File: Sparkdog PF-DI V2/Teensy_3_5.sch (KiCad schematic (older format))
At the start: 4 parts, among them U300 Teensy_3_5

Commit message: Commit schematic changes, new parts library footprints and step files, PCB design file.
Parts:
- D300, D301: footprint (none) -> Samacsys:RESC2012X60N
- RN300: footprint (none) -> Samacsys:742C083103JP
- U300: footprint (none) -> Sparkdog PF-DI V2:TEENSY_3_5
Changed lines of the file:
@@
 F 0 "U300" H 5675 9115 50  0000 C CNN
 F 1 "Teensy_3_5" H 5675 9024 50  0000 C CNN
-F 2 "" H 5100 5350 50  0001 C CNN
+F 2 "Sparkdog PF-DI V2:TEENSY_3_5" H 5100 5350 50  0001 C CNN
 F 3 "" H 5100 5350 50  0001 C CNN
 	1    5100 5350
@@
 F 0 "RN300" H 3938 5996 50  0000 L CNN
 F 1 "1206 1k" H 3938 5905 50  0000 L CNN
-F 2 "" V 4025 5950 50  0001 C CNN
+F 2 "Samacsys:742C083103JP" V 4025 5950 50  0001 C CNN
 F 3 "~" H 3750 5950 50  0001 C CNN
 	1    3750 5950
@@
 F 0 "D300" H 4193 6295 50  0000 C CNN
 F 1 "0805 LED" H 4193 6386 50  0000 C CNN
-F 2 "" H 4200 6550 50  0001 C CNN
+F 2 "Samacsys:RESC2012X60N" H 4200 6550 50  0001 C CNN
 F 3 "~" H 4200 6550 50  0001 C CNN
 	1    4200 6550
@@
 F 0 "D301" H 4193 6745 50  0000 C CNN
 F 1 "0805 LED" H 4193 6836 50  0000 C CNN
-F 2 "" H 4200 7000 50  0001 C CNN
+F 2 "Samacsys:RESC2012X60N" H 4200 7000 50  0001 C CNN
 F 3 "~" H 4200 7000 50  0001 C CNN
 	1    4200 7000

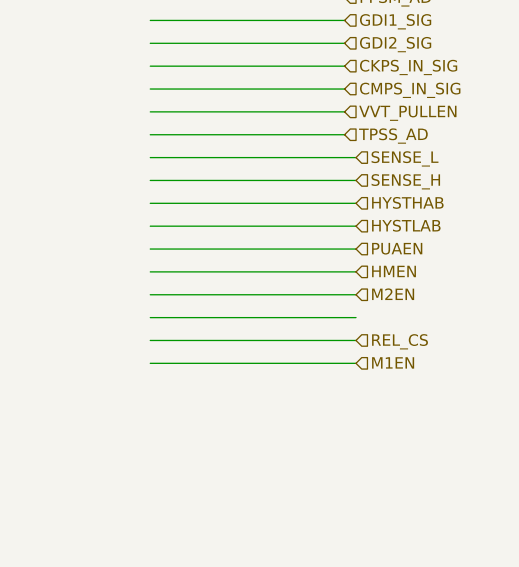
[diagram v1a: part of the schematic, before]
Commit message: Commit updates and Teensy schematic footprint correction.
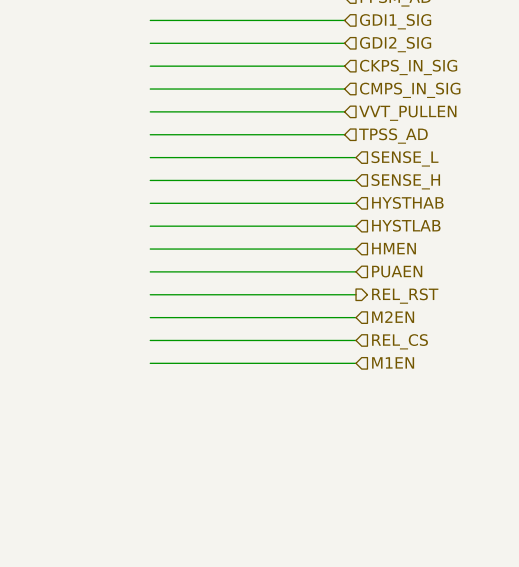
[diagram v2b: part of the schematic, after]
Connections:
- net labels added: REL_RST
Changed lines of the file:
@@
 Text HLabel 7350 4550 2    50   Input ~ 0
 HYSTLAB
+Text HLabel 7350 4750 2    50   Input ~ 0
+PUAEN
 Text HLabel 7350 4650 2    50   Input ~ 0
-PUAEN
-Text HLabel 7350 4750 2    50   Input ~ 0
 HMEN
-Text HLabel 7350 4850 2    50   Input ~ 0
+Text HLabel 7350 4950 2    50   Input ~ 0
 M2EN
 Text HLabel 7350 5050 2    50   Input ~ 0
@@
 Text HLabel 3000 4150 0    50   Output ~ 0
 U1_CTS
+Text HLabel 7350 4850 2    50   Output ~ 0
+REL_RST
 $EndSCHEMATC

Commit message: Commit for safekeeping
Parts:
- U300: symbol Rabbit~ECU~Schematic~Symbols:Teensy_3_5 -> Sparkdog-PF-DI-V2-rescue:Teensy_3_5-Rabbit_ECU_Schematic_Symbols
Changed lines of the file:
@@
 $EndDescr
 $Comp
-L Rabbit~ECU~Schematic~Symbols:Teensy_3_5 U300
+L Sparkdog-PF-DI-V2-rescue:Teensy_3_5-Rabbit_ECU_Schematic_Symbols U300
 U 1 1 605693EF
 P 5100 5350
+AR Path="/605693EF" Ref="U300"  Part="1"
+AR Path="/6056510E/605693EF" Ref="U300"  Part="1"
 F 0 "U300" H 5675 9115 50  0000 C CNN
 F 1 "Teensy_3_5" H 5675 9024 50  0000 C CNN

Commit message: Commit all files up to 21072021 Gerber and drill outputs.
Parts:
- removed U300: Teensy_3_5, Sparkdog PF-DI V2:TEENSY_3_5, symbol Sparkdog-PF-DI-V2-rescue:Teensy_3_5-Rabbit_ECU_Schematic_Symbols
- added U300: Teensy_3_5, Sparkdog PF-DI V2:TEENSY_3_5, symbol Rabbit~ECU~Schematic~Symbols:Teensy_3_5
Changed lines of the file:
@@
 Comment4 ""
 $EndDescr
-$Comp
-L Sparkdog-PF-DI-V2-rescue:Teensy_3_5-Rabbit_ECU_Schematic_Symbols U300
-U 1 1 605693EF
-P 5100 5350
-AR Path="/605693EF" Ref="U300"  Part="1"
-AR Path="/6056510E/605693EF" Ref="U300"  Part="1"
-F 0 "U300" H 5675 9115 50  0000 C CNN
-F 1 "Teensy_3_5" H 5675 9024 50  0000 C CNN
-F 2 "Sparkdog PF-DI V2:TEENSY_3_5" H 5100 5350 50  0001 C CNN
-F 3 "" H 5100 5350 50  0001 C CNN
-	1    5100 5350
-	1    0    0    -1
-$EndComp
 Text HLabel 3000 2450 0    50   Input ~ 0
 INJ1_SIG
@@
 Text HLabel 7350 4850 2    50   Output ~ 0
 REL_RST
+$Comp
+L Rabbit~ECU~Schematic~Symbols:Teensy_3_5 U300
+U 1 1 60F1A627
+P 5100 5350
+F 0 "U300" H 5725 9115 50  0000 C CNN
+F 1 "Teensy_3_5" H 5725 9024 50  0000 C CNN
+F 2 "Sparkdog PF-DI V2:TEENSY_3_5" H 5100 5350 50  0001 C CNN
+F 3 "" H 5100 5350 50  0001 C CNN
+	1    5100 5350
+	1    0    0    -1
+$EndComp
 $EndSCHEMATC
